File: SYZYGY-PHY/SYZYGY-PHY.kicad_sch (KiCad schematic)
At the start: 37 parts, among them J1 QTH-020-01-X-D-DP-A, J2 ARJM11C7-502-KB-EW2, J3 Conn_01x08, U1 GPY111, Y1 Crystal_GND24

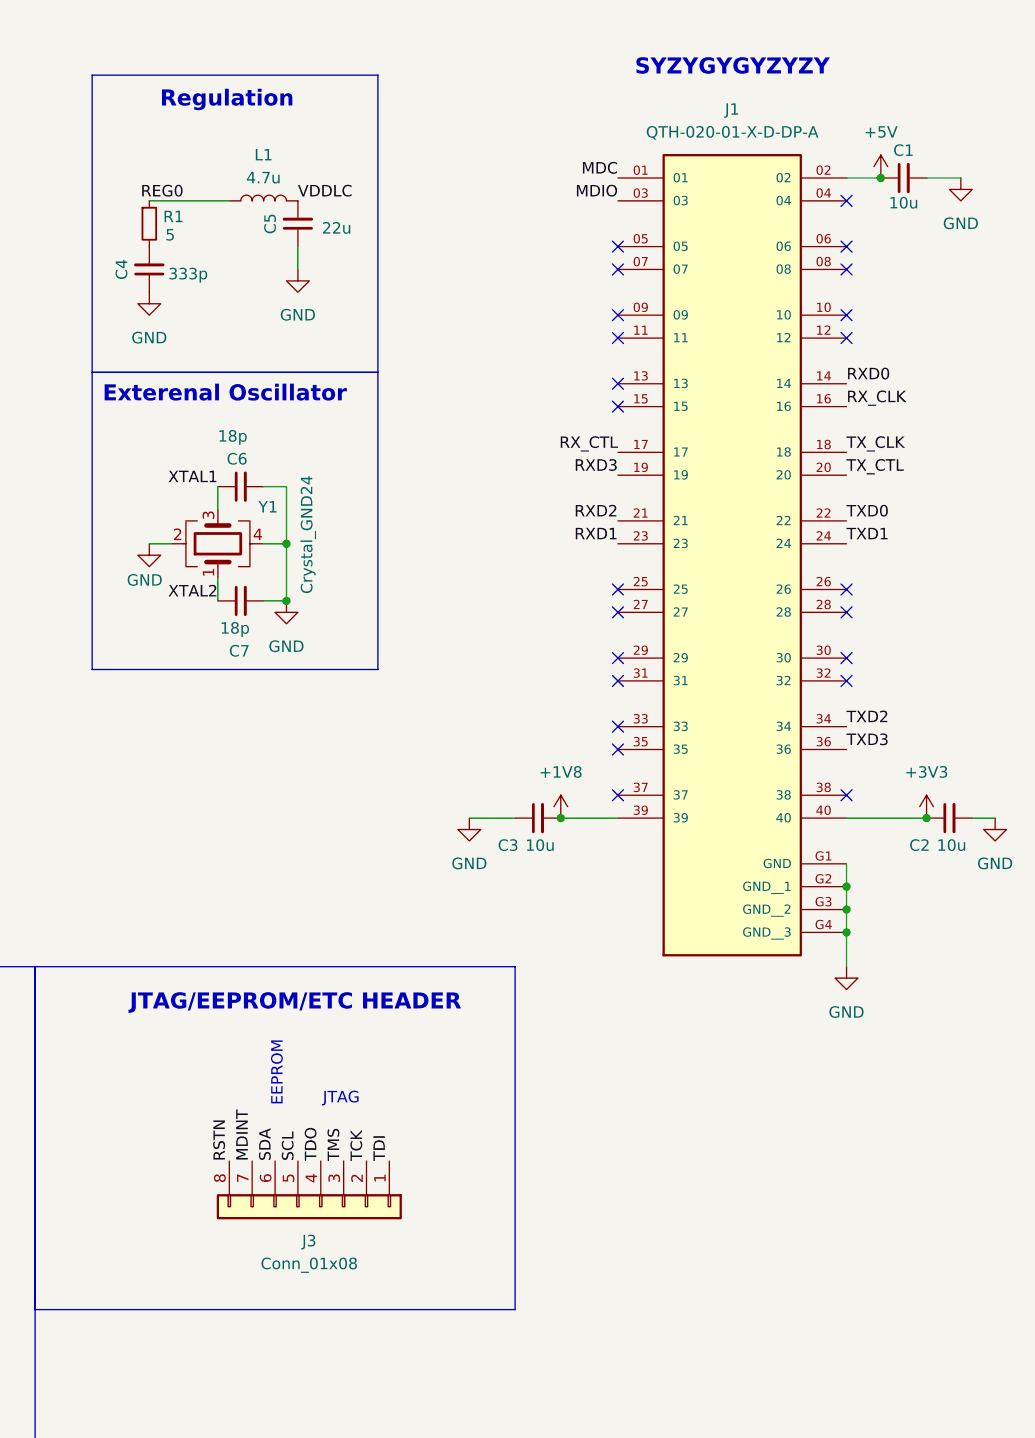
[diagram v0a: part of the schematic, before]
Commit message: picking a concrete inductor and updating footprint, breakout out MDC/MDIO into headers instead of SYZYGY, corrected rules and text labels
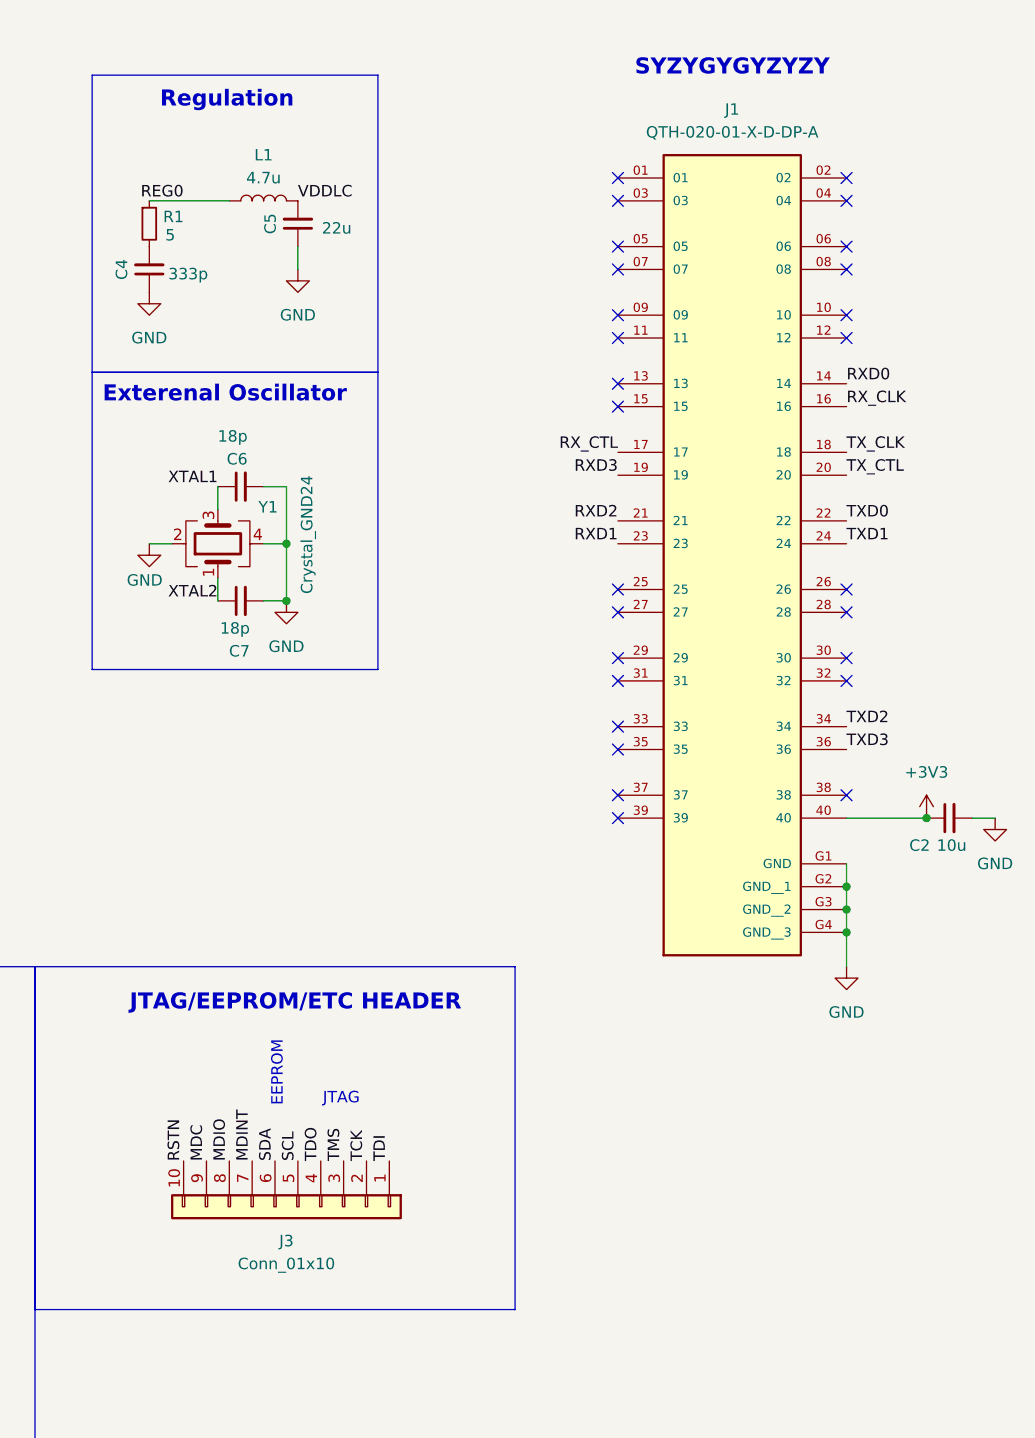
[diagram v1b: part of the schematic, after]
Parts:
- removed C1, C3: 10u, Capacitor_SMD:C_0805_2012Metric_Pad1.18x1.45mm_HandSolder, symbol Device:C_Small
- removed J3: Conn_01x08, Connector_PinSocket_2.54mm:PinSocket_1x08_P2.54mm_Vertical, symbol Connector_Generic:Conn_01x08
- added J3: Conn_01x10, Connector_PinSocket_2.54mm:PinSocket_1x10_P2.54mm_Vertical, symbol Connector_Generic:Conn_01x10
- L1: footprint Inductor_SMD:L_Abracon_ASPI-0425 -> Inductor_SMD:L_0805_2012Metric_Pad1.05x1.20mm_HandSolder; Part (none) -> MLZ2012N4R7LT000
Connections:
- net MDC: now also J3.9 (Pin_9); no longer J1.01
- net MDINT: now also J3.7 (Pin_7)
- net MDIO: now also J3.8 (Pin_8); no longer J1.03
- net RSTN: now also J3.10 (Pin_10)
- net SCL: now also J3.5 (Pin_5)
- net SDA: now also J3.6 (Pin_6)
- net TCK: now also J3.2 (Pin_2)
- net TDI: now also J3.1 (Pin_1)
- net TDO: now also J3.4 (Pin_4)
- net TMS: now also J3.3 (Pin_3)
- net +1V8: no longer names the net of J1.39
- net +5V: no longer names the net of J1.02
- no-connect marks 24 -> 28

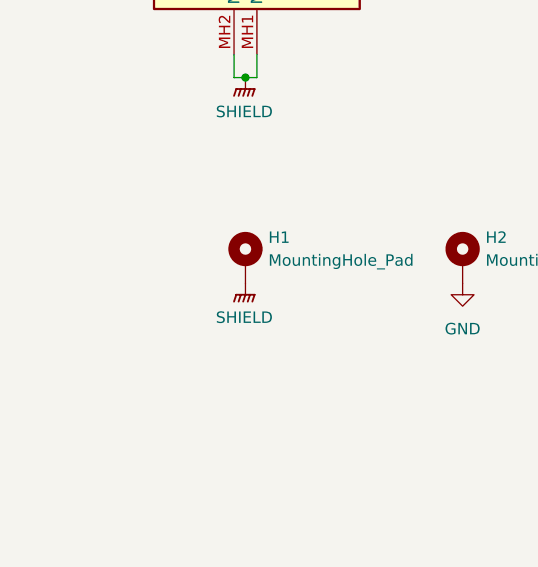
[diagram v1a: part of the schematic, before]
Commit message: adding another mounting hole for a more stable 3 mounts
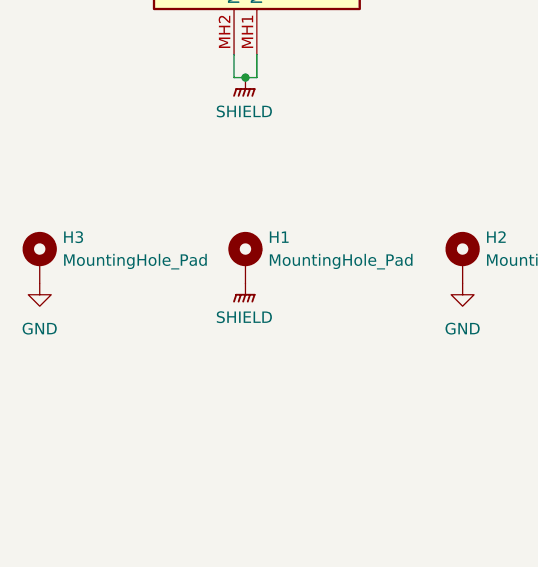
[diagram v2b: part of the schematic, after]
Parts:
- added H3: MountingHole_Pad, MountingHole:MountingHole_2.7mm_M2.5_Pad, symbol Mechanical:MountingHole_Pad
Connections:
- net GND: now also H3.1
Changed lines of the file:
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@@
+	)
+	(symbol
+		(lib_id "power:GND")
+		(at 22.86 144.78 0)
+		(unit 1)
+		(exclude_from_sim no)
+		(in_bom yes)
+		(on_board yes)
+		(dnp no)
+		(fields_autoplaced yes)
+		(property "Reference" "#PWR01"
+			(at 22.86 151.13 0)
+			(effects
+				(font
+					(size 1.27 1.27)
+				)
+				(hide yes)
+			)
+		)
+		(property "Value" "GND"
+			(at 22.86 149.86 0)
+			(effects
+				(font
+					(size 1.27 1.27)
+				)
+			)
+		)
+		(property "Footprint" ""
+			(at 22.86 144.78 0)
+			(effects
+				(font
+					(size 1.27 1.27)
+				)
+				(hide yes)
+			)
+		)
+		(property "Datasheet" ""
+			(at 22.86 144.78 0)
+			(effects
+				(font
+					(size 1.27 1.27)
+				)
+				(hide yes)
+			)
+		)
+		(property "Description" "Power symbol creates a global label with name \"GND\" , ground"
+			(at 22.86 144.78 0)
+			(effects
+				(font
+					(size 1.27 1.27)
+				)
+				(hide yes)
+			)
+		)
+		(pin "1"
+		)
+		(instances
+			(project "SYZYGY-PHY"
+				(path "/cd7d6255-0cd2-43fc-ba6e-5ac7b6205d5d"
+					(reference "#PWR01")
+					(unit 1)
+				)
+			)
+		)
 	)
 	(symbol
@@
 					(unit 1)
 				)
+			)
+		)
+	)
+	(symbol
+		(lib_id "Mechanical:MountingHole_Pad")
+		(at 22.86 142.24 0)
+		(unit 1)
+		(exclude_from_sim yes)
+		(in_bom no)
+		(on_board yes)
+		(dnp no)
+		(fields_autoplaced yes)
+		(property "Reference" "H3"
+			(at 25.4 139.6999 0)
+			(effects
+				(font
+					(size 1.27 1.27)
+				)
+				(justify left)
+			)
+		)
+		(property "Value" "MountingHole_Pad"
+			(at 25.4 142.2399 0)
+			(effects
+				(font
+					(size 1.27 1.27)
+				)
+				(justify left)
+			)
+		)
+		(property "Footprint" "MountingHole:MountingHole_2.7mm_M2.5_Pad"
+			(at 22.86 142.24 0)
+			(effects
+				(font
+					(size 1.27 1.27)
+				)
+				(hide yes)
+			)
+		)
+		(property "Datasheet" "~"
+			(at 22.86 142.24 0)
+			(effects
+				(font
+					(size 1.27 1.27)
+				)
+				(hide yes)
+			)
+		)
+		(property "Description" "Mounting Hole with connection"
+			(at 22.86 142.24 0)
+			(effects
+				(font
+					(size 1.27 1.27)
+				)
+				(hide yes)
+			)
+		)
+		(pin "1"
+		)
+		(instances
+			(project "SYZYGY-PHY"
+				(path "/cd7d6255-0cd2-43fc-ba6e-5ac7b6205d5d"
+					(reference "H3")
+					(unit 1)
+				)

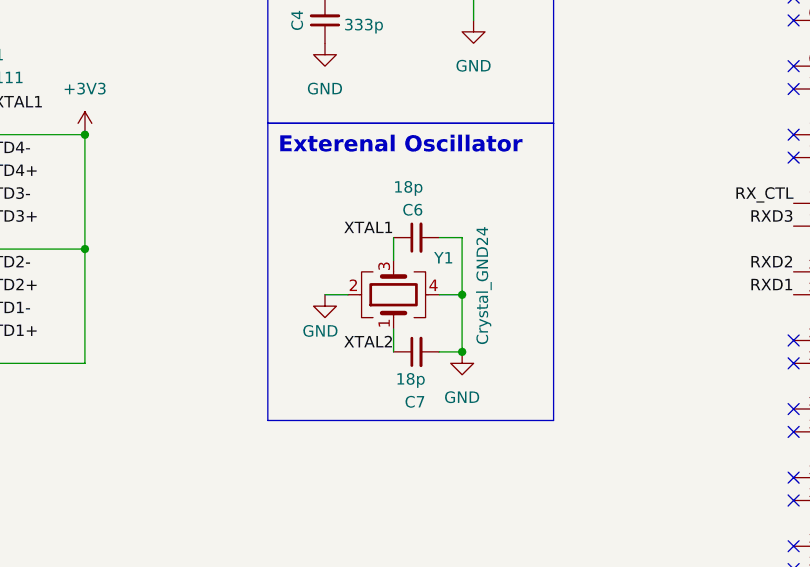
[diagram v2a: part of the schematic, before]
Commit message: updating the caps and crystal, confirming the crystal circuit and footprints
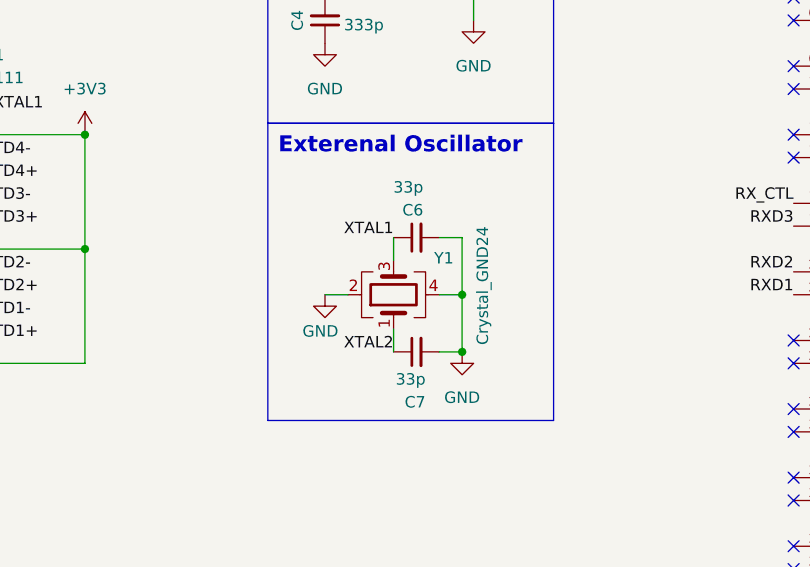
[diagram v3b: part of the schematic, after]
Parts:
- C6, C7: value 18p -> 33p
- Y1: Mouser (none) -> FA-238 25.0000MB-I
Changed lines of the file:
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@@
 			)
 		)
-		(property "Value" "18p"
+		(property "Value" "33p"
 			(at 192.786 81.788 90)
 			(effects
@@
 			)
 		)
-		(property "Value" "18p"
+		(property "Value" "33p"
 			(at 192.532 60.452 90)
 			(effects
@@
 			)
 		)
-		(property "Datasheet" "~"
+		(property "Datasheet" "https://www.mouser.com/datasheet/2/137/FA_238_en-932914.pdf"
 			(at 189.23 72.39 0)
 			(effects
@@
 			(effects
 				(font
+					(size 1.27 1.27)
+				)
+				(hide yes)
+			)
+		)
+		(property "Mouser" "FA-238 25.0000MB-I "
+			(at 189.23 72.39 90)
+			(effects
+				(font

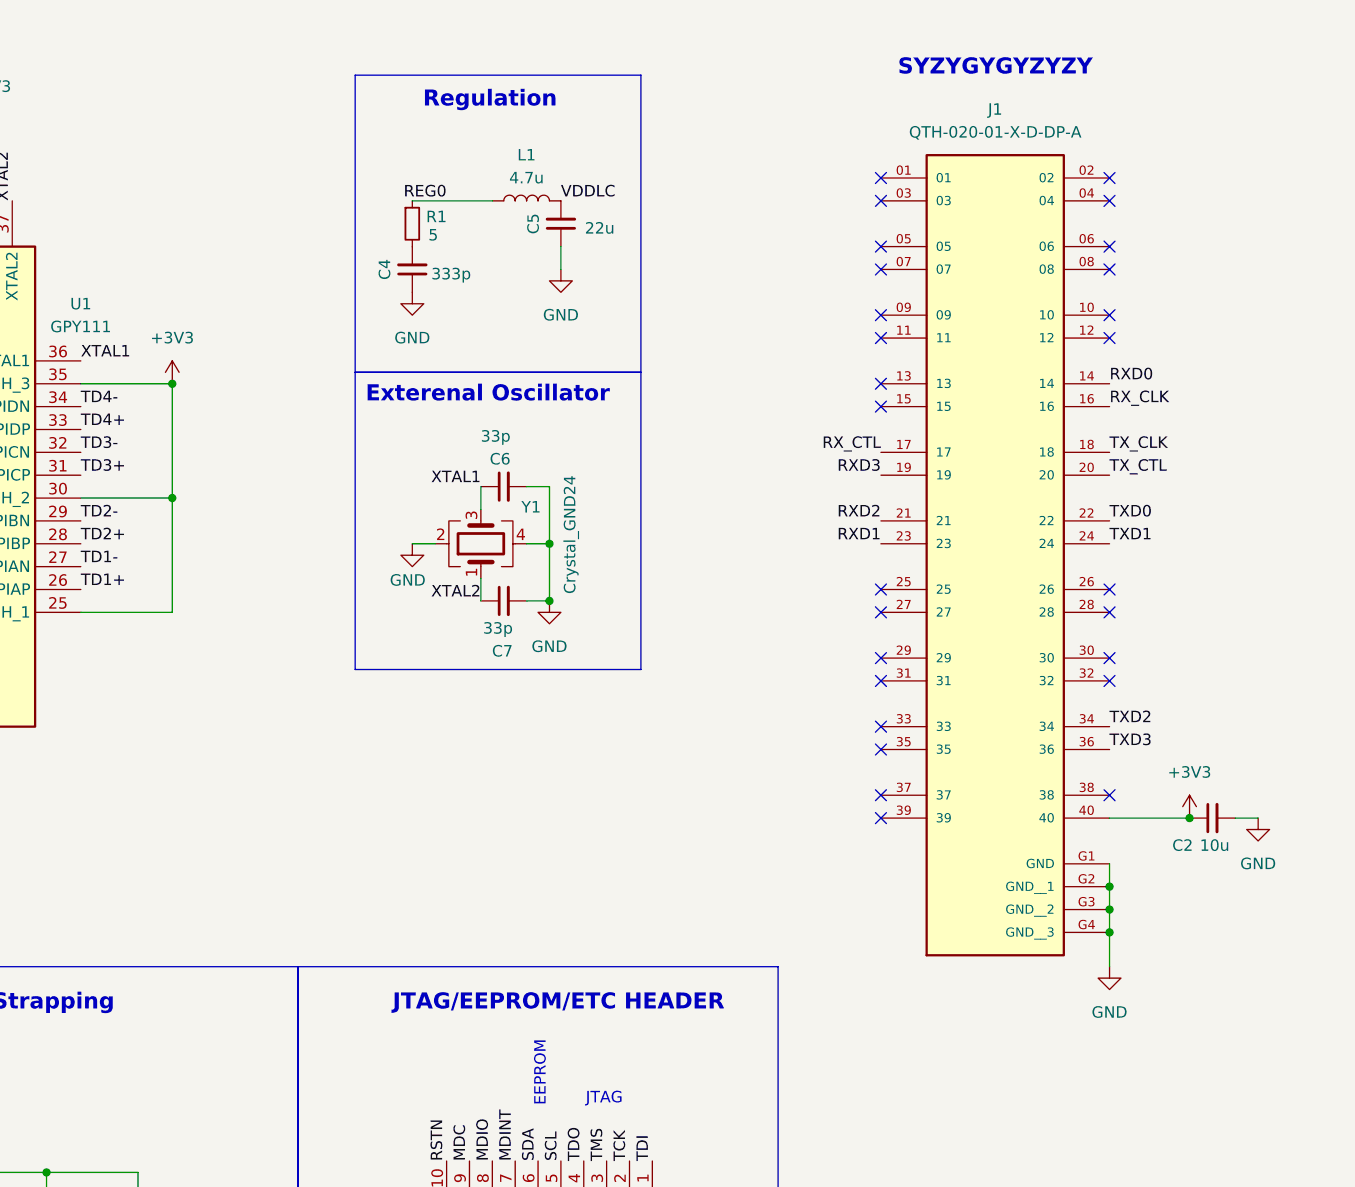
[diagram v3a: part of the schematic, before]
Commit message: adding level shifter parts to schematic and pcb, rerouted RGMII and mostly length matched each channel
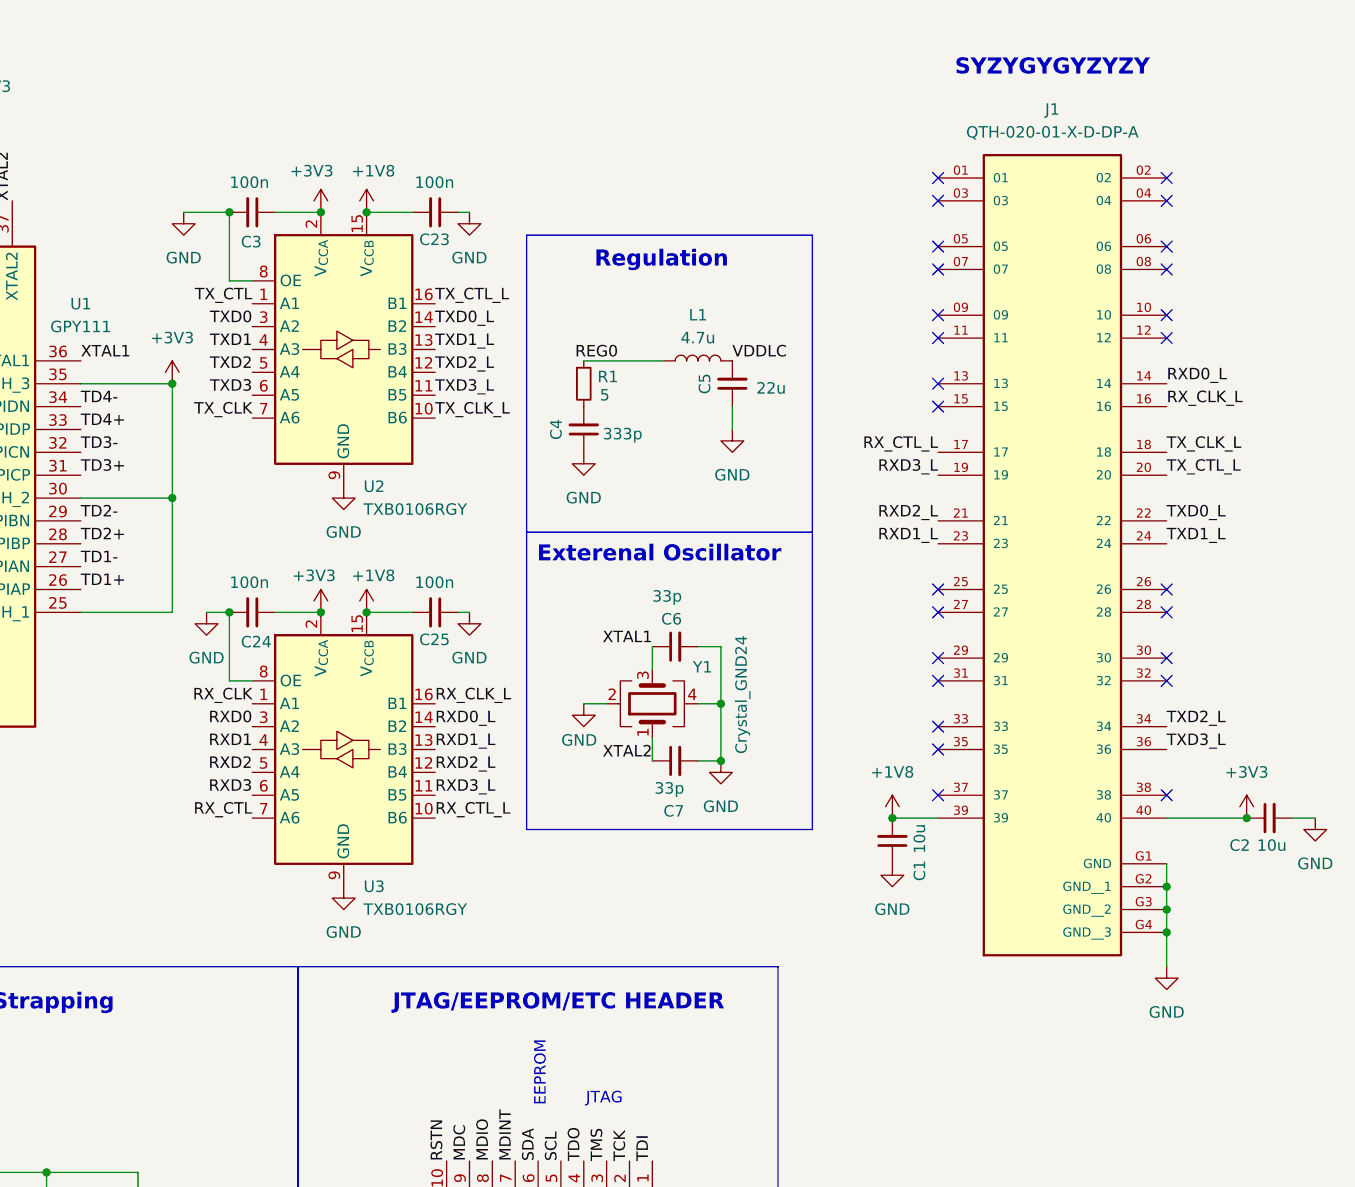
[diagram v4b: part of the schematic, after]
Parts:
- added C1: 10u, Capacitor_SMD:C_0805_2012Metric_Pad1.18x1.45mm_HandSolder, symbol Device:C_Small
- added C23, C24, C25, C3: 100n, Capacitor_SMD:C_0805_2012Metric_Pad1.18x1.45mm_HandSolder, symbol Device:C_Small
- added U2, U3: TXB0106RGY, local:TXV0106BQBR, symbol Logic_LevelTranslator:TXB0106RGY
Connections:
- net +3V3: now also C24.1, C3.1, U2.2 (V_{CCA}), U3.2 (V_{CCA})
- net GND: now also C1.1, C23.1, C24.2, C25.1, C3.2, U2.17 (GND), U2.8 (OE), U2.9 (GND), U3.17 (GND), U3.8 (OE), U3.9 (GND)
- net RXD0: now also U3.3 (A2); no longer J1.14
- net RXD1: now also U3.4 (A3); no longer J1.23
- net RXD2: now also U3.5 (A4); no longer J1.21
- net RXD3: now also U3.6 (A5); no longer J1.19
- net RX_CLK: now also U3.1 (A1); no longer J1.16
- net RX_CTL: now also U3.7 (A6); no longer J1.17
- net TXD0: now also U2.3 (A2); no longer J1.22
- net TXD1: now also U2.4 (A3); no longer J1.24
- net TXD2: now also U2.5 (A4); no longer J1.34
- net TXD3: now also U2.6 (A5); no longer J1.36
- net TX_CLK: now also U2.7 (A6); no longer J1.18
- net TX_CTL: now also U2.1 (A1); no longer J1.20
- net +1V8: now reaches J1.39
- net +1V8: now also C1.2, C23.2, C25.2, U2.15 (V_{CCB}), U3.15 (V_{CCB})
- new net RXD0_L: J1.14, U3.14 (B2)
- new net RXD1_L: J1.23, U3.13 (B3)
- new net RXD2_L: J1.21, U3.12 (B4)
- new net RXD3_L: J1.19, U3.11 (B5)
- new net RX_CLK_L: J1.16, U3.16 (B1)
- new net RX_CTL_L: J1.17, U3.10 (B6)
- new net TXD0_L: J1.22, U2.14 (B2)
- new net TXD1_L: J1.24, U2.13 (B3)
- new net TXD2_L: J1.34, U2.12 (B4)
- new net TXD3_L: J1.36, U2.11 (B5)
- new net TX_CLK_L: J1.18, U2.10 (B6)
- new net TX_CTL_L: J1.20, U2.16 (B1)
- no-connect marks 28 -> 27
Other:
- moved on the sheet: C2, C4, C5, C6, C7, J1, L1, R1, Y1
